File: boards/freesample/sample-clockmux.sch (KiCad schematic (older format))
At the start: 0 parts

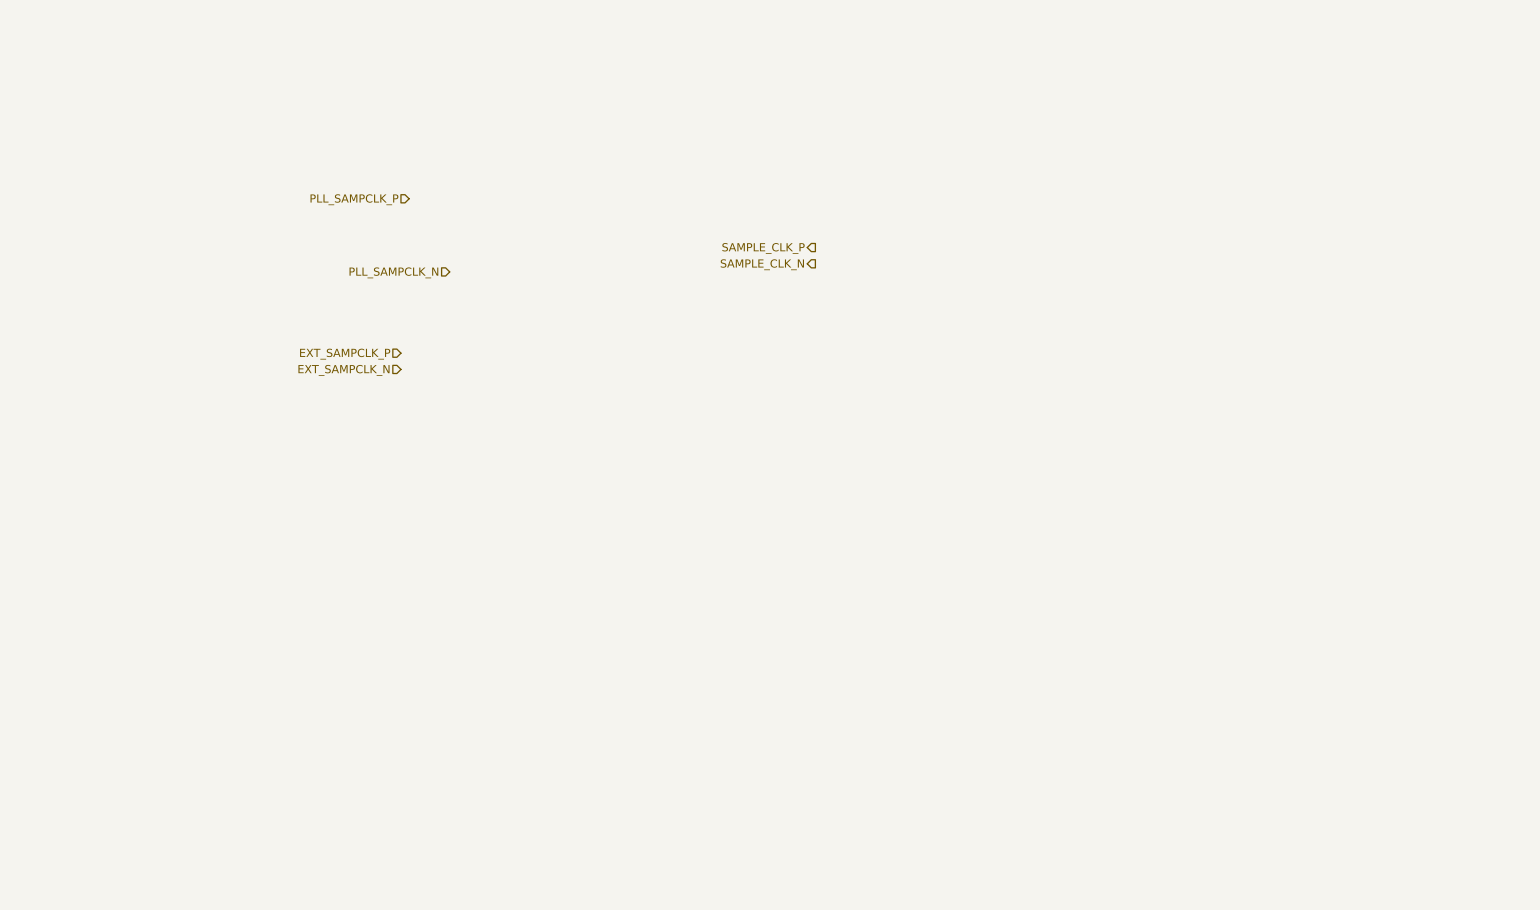
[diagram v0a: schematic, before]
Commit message: Continued initial schematic capture
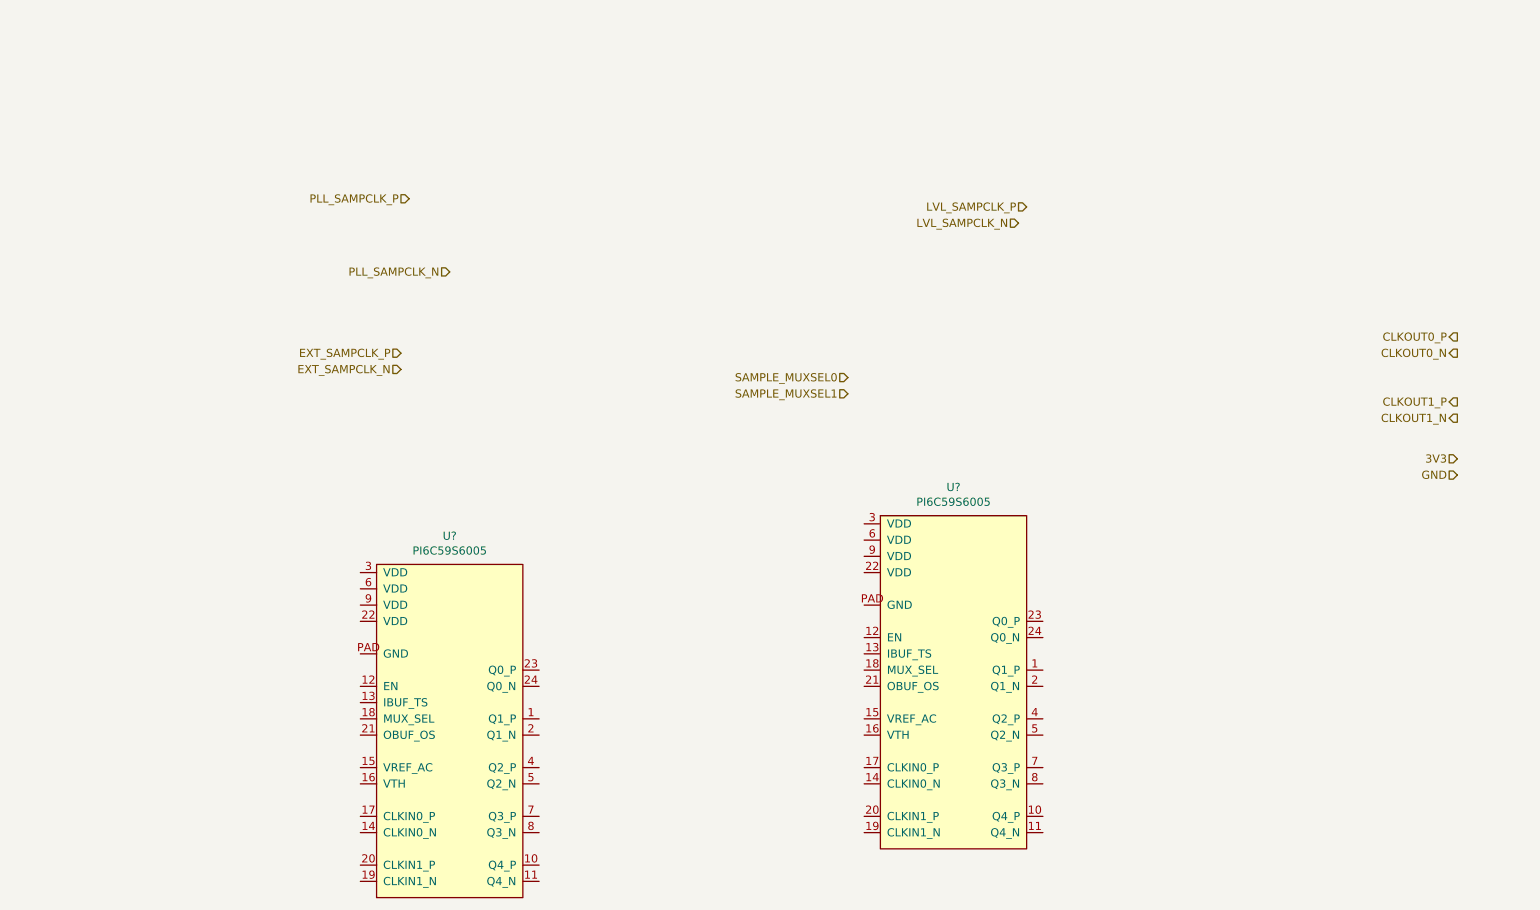
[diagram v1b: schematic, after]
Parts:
- added U? (x2): PI6C59S6005, symbol special-azonenberg:PI6C59S6005
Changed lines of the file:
@@
 $Descr A4 11693 8268
 encoding utf-8
-Sheet 11 11
-Title ""
-Date ""
-Rev ""
-Comp ""
+Sheet 11 12
+Title "FREESAMPLE Oscilloscope"
+Date "2018-12-17"
+Rev "0.1"
+Comp "Andrew D. Zonenberg / Antikernel Labs"
 Comment1 ""
 Comment2 ""
@@
 Text HLabel 3000 2750 0    50   Input ~ 0
 EXT_SAMPCLK_N
-Text HLabel 5550 2000 0    50   Output ~ 0
-SAMPLE_CLK_P
-Text HLabel 5550 2100 0    50   Output ~ 0
-SAMPLE_CLK_N
+Text HLabel 6850 1750 0    50   Input ~ 0
+LVL_SAMPCLK_P
+Text HLabel 6800 1850 0    50   Input ~ 0
+LVL_SAMPCLK_N
+Text HLabel 5750 2800 0    50   Input ~ 0
+SAMPLE_MUXSEL0
+Text HLabel 5750 2900 0    50   Input ~ 0
+SAMPLE_MUXSEL1
+$Comp
+L special-azonenberg:PI6C59S6005 U?
+U 1 1 5C3D401A
+P 2850 6000
+F 0 "U?" H 3300 8225 50  0000 C CNN
+F 1 "PI6C59S6005" H 3300 8134 50  0000 C CNN
+F 2 "" H 2850 5700 50  0001 C CNN
+F 3 "" H 2850 5700 50  0001 C CNN
+	1    2850 6000
+	1    0    0    -1
+$EndComp
+$Comp
+L special-azonenberg:PI6C59S6005 U?
+U 1 1 5C3D4D31
+P 5950 5700
+F 0 "U?" H 6400 7925 50  0000 C CNN
+F 1 "PI6C59S6005" H 6400 7834 50  0000 C CNN
+F 2 "" H 5950 5400 50  0001 C CNN
+F 3 "" H 5950 5400 50  0001 C CNN
+	1    5950 5700
+	1    0    0    -1
+$EndComp
+Text HLabel 9500 2550 0    50   Output ~ 0
+CLKOUT0_P
+Text HLabel 9500 2650 0    50   Output ~ 0
+CLKOUT0_N
+Text HLabel 9500 2950 0    50   Output ~ 0
+CLKOUT1_P
+Text HLabel 9500 3050 0    50   Output ~ 0
+CLKOUT1_N
+Text HLabel 9500 3300 0    50   Input ~ 0
+3V3
+Text HLabel 9500 3400 0    50   Input ~ 0
+GND
 $EndSCHEMATC

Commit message: Continued work on schematic capture
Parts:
- added C145, C158: 4.7 uF, symbol device:C
- added C146, C147, C148, C149, C155, C156: 0.1 uF, symbol device:C
- added C150, C151, C152, C153, C159, C160, C161, C162: 0.47 uF, symbol device:C
- added C154, C157: 0.01 uF, symbol device:C
- added JP2, JP3: JUMPER_0402, symbol special-azonenberg:JUMPER_0402_SPDT
- gave numbers to parts that had none: 2
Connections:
- net 3V3: now also U11.12 (EN), U11.22 (VDD), U11.3 (VDD), U11.6 (VDD), U11.9 (VDD), U12.12 (EN), U12.22 (VDD), U12.3 (VDD), U12.6 (VDD), U12.9 (VDD), C145.1, C150.1, C151.1, C152.1, C153.1, C154.2, C157.2, C158.1, C159.1, C160.1, C161.1, C162.1, JP2.1, JP3.1
- net CLKOUT0_N: now also U12.24 (Q0_N)
- net CLKOUT0_P: now also U12.23 (Q0_P)
- net CLKOUT1_N: now also U12.2 (Q1_N)
- net CLKOUT1_P: now also U12.1 (Q1_P)
- net EXT_SAMPCLK_N: now also C149.2
- net EXT_SAMPCLK_P: now also C148.2
- net GND: now also U11.21 (OBUF_OS), U11.PAD (GND), U12.21 (OBUF_OS), U12.PAD (GND), C145.2, C150.2, C151.2, C152.2, C153.2, C158.2, C159.2, C160.2, C161.2, C162.2, JP2.3, JP3.3
- net LVL_SAMPCLK_N: now also C147.2
- net LVL_SAMPCLK_P: now also C146.2
- net SAMPLE_MUXSEL0: now also U11.18 (MUX_SEL)
- net SAMPLE_MUXSEL1: now also U12.18 (MUX_SEL)
- net BUF2_IN_SEL: now reaches U11.13 (IBUF_TS)
- net BUF2_IN_SEL: now also JP2.2
- net LVL_CLK_AC_N: now reaches U11.14 (CLKIN0_N)
- net LVL_CLK_AC_N: now also C147.1
- net at U11.15 (VREF_AC): now also U11.16 (VTH), C154.1
- net LVL_CLK_AC_P: now reaches U11.17 (CLKIN0_P)
- net LVL_CLK_AC_P: now also C146.1
- net EXT_CLK_AC_N: now reaches U11.19 (CLKIN1_N)
- net EXT_CLK_AC_N: now also C149.1
- net EXT_CLK_AC_P: now reaches U11.20 (CLKIN1_P)
- net EXT_CLK_AC_P: now also C148.1
- net MUXCLK0_P: now reaches U11.23 (Q0_P)
- net MUXCLK0_P: now also C155.2
- net MUXCLK0_N: now reaches U11.24 (Q0_N)
- net MUXCLK0_N: now also C156.2
- net BUF3_IN_SEL: now reaches U12.13 (IBUF_TS)
- net BUF3_IN_SEL: now also JP3.2
- net MUXCLK0_AC_N: now reaches U12.14 (CLKIN0_N)
- net MUXCLK0_AC_N: now also C156.1
- net at U12.15 (VREF_AC): now also U12.16 (VTH), C157.1
- net MUXCLK0_AC_P: now reaches U12.17 (CLKIN0_P)
- net MUXCLK0_AC_P: now also C155.1
- no-connect marks 0 -> 14
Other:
- moved on the sheet: U11, U12

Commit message: Continued work on FREESAMPLE schematic including PSU.
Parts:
- added C205, C206: 0.1 uF, symbol device:C
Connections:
- net PLL_SAMPCLK_N: now also C206.2
- net PLL_SAMPCLK_P: now also C205.2
- net MUXCLK1_AC_N: now reaches U12.19 (CLKIN1_N)
- net MUXCLK1_AC_N: now also C206.1
- net MUXCLK1_AC_P: now reaches U12.20 (CLKIN1_P)
- net MUXCLK1_AC_P: now also C205.1
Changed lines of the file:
@@
 Sheet 11 12
 Title "FREESAMPLE Oscilloscope"
-Date "2018-12-17"
+Date "2019-02-23"
 Rev "0.1"
 Comp "Andrew D. Zonenberg / Antikernel Labs"
@@
 Comment4 ""
 $EndDescr
-Text HLabel 5450 3150 0    50   Input ~ 0
+Text HLabel 4400 3150 0    50   Input ~ 0
 PLL_SAMPCLK_P
-Text HLabel 5450 3250 0    50   Input ~ 0
+Text HLabel 4400 3250 0    50   Input ~ 0
 PLL_SAMPCLK_N
 Text HLabel 1350 3200 0    50   Input ~ 0
@@
 	5200 2550 5500 2550
 Connection ~ 5500 2550
+$Comp
+L device:C C205
+U 1 1 5CB05D09
+P 4650 3100
+F 0 "C205" V 4700 3250 50  0000 C CNN
+F 1 "0.1 uF" V 4600 3300 50  0000 C CNN
+F 2 "" H 4688 2950 50  0001 C CNN
+F 3 "" H 4650 3100 50  0001 C CNN
+	1    4650 3100
+	0    1    -1   0
+$EndComp
+$Comp
+L device:C C206
+U 1 1 5CB05D13
+P 4650 3300
+F 0 "C206" V 4700 3450 50  0000 C CNN
+F 1 "0.1 uF" V 4600 3500 50  0000 C CNN
+F 2 "" H 4688 3150 50  0001 C CNN
+F 3 "" H 4650 3300 50  0001 C CNN
+	1    4650 3300
+	0    1    -1   0
+$EndComp
+Wire Wire Line
+	4400 3150 4500 3150
+Wire Wire Line
+	4500 3150 4500 3100
+Wire Wire Line
+	4400 3250 4500 3250
+Wire Wire Line
+	4500 3250 4500 3300
+Wire Wire Line
+	4800 3100 5600 3100
+Wire Wire Line
+	5600 3100 5600 3150
+Wire Wire Line
+	4800 3300 5600 3300
+Wire Wire Line
+	5600 3300 5600 3250
+Text Label 4950 3100 0    50   ~ 0
+MUXCLK1_AC_P
+Text Label 4950 3300 0    50   ~ 0
+MUXCLK1_AC_N
 $EndSCHEMATC

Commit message: Finished PSU schematic. Ready for design review!
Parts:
- added J15, J16: SMA, symbol Connector:Conn_Coaxial
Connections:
- net GND: now also J15.2 (Ext), J16.2 (Ext)
- net CLKOUT2_P: now reaches U12.4 (Q2_P)
- net CLKOUT2_P: now also J15.1 (In)
- net CLKOUT2_N: now reaches U12.5 (Q2_N)
- net CLKOUT2_N: now also J16.1 (In)
- no-connect marks 14 -> 12
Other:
- note added: "Muxed clock/trigger signal for debugging\nor external DAQ hardware"
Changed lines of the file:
@@
 Sheet 11 12
 Title "FREESAMPLE Oscilloscope"
-Date "2019-03-10"
+Date "2019-03-11"
 Rev "0.1"
 Comp "Andrew D. Zonenberg / Antikernel Labs"
@@
 Text Label 5600 2350 2    50   ~ 0
 GND
-NoConn ~ 6700 2550
-NoConn ~ 6700 2650
 NoConn ~ 6700 2850
 NoConn ~ 6700 2950
@@
 Text Label 4950 3300 0    50   ~ 0
 MUXCLK1_AC_N
+$Comp
+L Connector:Conn_Coaxial J16
+U 1 1 5D26866A
+P 7650 2700
+F 0 "J16" H 7750 2675 50  0000 L CNN
+F 1 "SMA" H 7750 2584 50  0000 L CNN
+F 2 "" H 7650 2700 50  0001 C CNN
+F 3 "" H 7650 2700 50  0001 C CNN
+	1    7650 2700
+	1    0    0    -1
+$EndComp
+$Comp
+L Connector:Conn_Coaxial J15
+U 1 1 5D268D26
+P 7650 2500
+F 0 "J15" H 7750 2382 50  0000 L CNN
+F 1 "SMA" H 7750 2473 50  0000 L CNN
+F 2 "" H 7650 2500 50  0001 C CNN
+F 3 "" H 7650 2500 50  0001 C CNN
+	1    7650 2500
+	1    0    0    1
+$EndComp
+Wire Wire Line
+	6700 2550 7500 2550
+Wire Wire Line
+	7500 2550 7500 2500
+Wire Wire Line
+	6700 2650 7500 2650
+Wire Wire Line
+	7500 2650 7500 2700
+Text Label 7650 2300 0    50   ~ 0
+GND
+Text Label 7650 2900 0    50   ~ 0
+GND
+Text Label 6750 2550 0    50   ~ 0
+CLKOUT2_P
+Text Label 6750 2650 0    50   ~ 0
+CLKOUT2_N
+Text Notes 8000 2650 0    50   ~ 0
+Muxed clock/trigger signal for debugging\nor external DAQ hardware
 $EndSCHEMATC

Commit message: Specified part number for AC coupling caps
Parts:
- C146, C147, C148, C149, C155, C156, C205, C206: value 0.1 uF -> 530Z104KT10T
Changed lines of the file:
@@
 Sheet 11 12
 Title "FREESAMPLE Oscilloscope"
-Date "2019-03-11"
+Date "2019-03-13"
 Rev "0.1"
 Comp "Andrew D. Zonenberg / Antikernel Labs"
 Comment1 "Ready for review"
-Comment2 ""
+Comment2 "Ready for review"
 Comment3 ""
 Comment4 ""
@@
 P 1500 3200
 F 0 "C149" V 1400 3000 50  0000 C CNN
-F 1 "0.1 uF" V 1450 3400 50  0000 C CNN
+F 1 "530Z104KT10T" V 2050 2800 50  0000 C CNN
 F 2 "" H 1538 3050 50  0001 C CNN
 F 3 "" H 1500 3200 50  0001 C CNN
@@
 P 1500 2800
 F 0 "C146" V 1550 2950 50  0000 C CNN
-F 1 "0.1 uF" V 1450 3000 50  0000 C CNN
+F 1 "530Z104KT10T" V 1950 2400 50  0000 C CNN
 F 2 "" H 1538 2650 50  0001 C CNN
 F 3 "" H 1500 2800 50  0001 C CNN
@@
 P 1500 3100
 F 0 "C148" V 1550 3250 50  0000 C CNN
-F 1 "0.1 uF" V 1450 3300 50  0000 C CNN
+F 1 "530Z104KT10T" V 2050 2700 50  0000 C CNN
 F 2 "" H 1538 2950 50  0001 C CNN
 F 3 "" H 1500 3100 50  0001 C CNN
@@
 P 1500 2900
 F 0 "C147" V 1400 2750 50  0000 C CNN
-F 1 "0.1 uF" V 1450 3100 50  0000 C CNN
+F 1 "530Z104KT10T" V 1950 2500 50  0000 C CNN
 F 2 "" H 1538 2750 50  0001 C CNN
 F 3 "" H 1500 2900 50  0001 C CNN
@@
 P 4350 1800
 F 0 "C155" V 4400 1950 50  0000 C CNN
-F 1 "0.1 uF" V 4300 2000 50  0000 C CNN
+F 1 "530Z104KT10T" V 4500 1800 50  0000 C CNN
 F 2 "" H 4388 1650 50  0001 C CNN
 F 3 "" H 4350 1800 50  0001 C CNN
@@
 P 4350 2050
 F 0 "C156" V 4400 2200 50  0000 C CNN
-F 1 "0.1 uF" V 4300 2250 50  0000 C CNN
+F 1 "530Z104KT10T" V 4200 2050 50  0000 C CNN
 F 2 "" H 4388 1900 50  0001 C CNN
 F 3 "" H 4350 2050 50  0001 C CNN
@@
 P 4650 3100
 F 0 "C205" V 4700 3250 50  0000 C CNN
-F 1 "0.1 uF" V 4600 3300 50  0000 C CNN
+F 1 "530Z104KT10T" V 4300 3350 50  0000 C CNN
 F 2 "" H 4688 2950 50  0001 C CNN
 F 3 "" H 4650 3100 50  0001 C CNN
@@
 P 4650 3300
 F 0 "C206" V 4700 3450 50  0000 C CNN
-F 1 "0.1 uF" V 4600 3500 50  0000 C CNN
+F 1 "530Z104KT10T" V 4400 3550 50  0000 C CNN
 F 2 "" H 4688 3150 50  0001 C CNN
 F 3 "" H 4650 3300 50  0001 C CNN
